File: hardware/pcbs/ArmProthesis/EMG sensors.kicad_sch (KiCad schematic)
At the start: 25 parts, among them IC1 INA128, U1 OPA2188AIDR, U4 OPA188AIDR

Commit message: BMS v0.3 + main folder reconstruction
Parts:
- removed C1: 8.2nF, Capacitor_SMD:C_0603_1608Metric_Pad1.08x0.95mm_HandSolder, symbol Device:C
- removed C2: 1uF, Capacitor_SMD:C_0603_1608Metric_Pad1.08x0.95mm_HandSolder, symbol Device:C
- removed D1, D3: BAT54W, Package_TO_SOT_SMD:SOT-323_SC-70, symbol Diode:BAT54W
- removed U1: OPA2188AIDR, OP AMPS:ОПА2188AIDR, symbol OP AMPS:OPA2188AIDR
- removed U3: ~, Connector_JST:JST_GH_BM02B-GHS-TBT_1x02-1MP_P1.25mm_Vertical, symbol headers:H_2
- removed U4: OPA188AIDR, OP AMPS:OPA188, symbol OP AMPS:OPA188AIDR
- removed U5: ~, Connector_JST:JST_GH_BM03B-GHS-TBT_1x03-1MP_P1.25mm_Vertical, symbol headers:H_3
- removed U6, U7, U8: ~, EMG:EMG_Snap_4mm, symbol headers:H_1
- added C10, C11, C6, C7, C8, C9: 1uF, Capacitor_SMD:C_0603_1608Metric_Pad1.08x0.95mm_HandSolder, symbol Device:C
- added D1, D3: BAT54J, Diode_SMD:D_SOD-323F, symbol Diode:BAT54J
- added J2, J4: Conn_01x01_Pin, Connectors:DIN_Male_1PIN_1.5mm, symbol Connector:Conn_01x01_Pin
- added J3: Conn_01x03_Pin, Connector_JST:JST_GH_SM03B-GHS-TB_1x03-1MP_P1.25mm_Horizontal, symbol Connector:Conn_01x03_Pin
- added R11: 1M, Resistor_SMD:R_0603_1608Metric_Pad0.98x0.95mm_HandSolder, symbol Device:R
- added U1, U2: ~, EMG:EMG_Snap_4mm, symbol headers:H_1
- added U6: OPA2188AIDR, OP AMPS:ОПА2188AIDR, symbol OP AMPS:OPA2188AIDR
- added U7: OPA188AIDR, OP AMPS:OPA188, symbol OP AMPS:OPA188AIDR
- C3: value 1uF -> 8.2nF; Website https://www.digikey.in/en/products/detail/kyocera-avx/KGM15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 -> https://eu.mouser.com/ProductDetail/KEMET/C0603X822F5JACTU?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
- IC1: footprint OP AMPS:INA128 -> OP AMPS:INA128U
- R1: value 200 -> 10M
- R2: value 10k -> 10M; Website (none) -> https://eu.mouser.com/ProductDetail/TE-Connectivity-Holswor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
- R3: value 10M -> 200
- R5: value 10M -> 10k; Website https://eu.mouser.com/ProductDetail/TE-Connectivity-Holswor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 -> (none)
- R8: value 10k -> 20k
- R9: value 20k -> 10k
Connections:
- net +5.5V: now also C6.1, C7.1, C8.1, J3.1 (Pin_1), U6.8 (V+), U7.7 (V+); no longer C3.1
- net -5.5V: now also C10.1, C11.1, C9.1, J3.2 (Pin_2), U6.4 (V-), U7.4 (V-); no longer C4.1
- net AEMG: now also R10.2, J4.1 (Pin_1), U7.6 (OUT); no longer R10.1
- net GND: now also R1.1, R2.2, C10.2, C11.2, C6.2, C7.2, C8.2, C9.2, J3.3 (Pin_3), R11.1, U6.3 (+INA), U6.5 (+INB), U7.3 (+IN); no longer C4.2, R3.1, R5.2
- net INVERTED: now also R6.1, R8.2, U6.1 (OUTA); no longer R6.2, R9.2
- net Vin1: now also R1.2, U1.1; no longer R3.2
- net Vin2: now also R2.1, U2.1; no longer R5.1
- net at R7.1: now also R9.1, D3.1 (K); no longer R8.2
- net at R7.2: now also R6.2, D1.2 (A), U6.6 (-INB); no longer R6.1
- net at IC1.1: now also R3.2; no longer R1.2
- net at IC1.6: now also R4.1; no longer R2.1
- net at IC1.8: now also R3.1; no longer R1.1
- net at R4.2: now also C3.1, C4.2
- net at VR1.1, VR1.2: now also R5.1, U6.2 (-INA); no longer R4.1
- new net: J2.1 (Pin_1), R11.2
- new net: D1.1 (K), D3.2 (A), U6.7 (OUTB)
- new net: R10.1, R8.1, R9.2, U7.2 (-IN)
- new net: C4.1, R5.2

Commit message: .
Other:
- note added: "Amplifiers"
- note added: "Decoupling capacitors for each amplifier"
- note added: "Headers and connectors"
- moved on the sheet: C10, C11, C6, C7, C8, C9, J2, J3, J4, R11, U1, U2

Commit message: .
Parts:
- removed C3: 8.2nF, Capacitor_SMD:C_0603_1608Metric_Pad1.08x0.95mm_HandSolder, symbol Device:C
- removed C4: 1uF, Capacitor_SMD:C_0603_1608Metric_Pad1.08x0.95mm_HandSolder, symbol Device:C
- removed U7: OPA188AIDR, OP AMPS:OPA188, symbol OP AMPS:OPA188AIDR
- added C1: 250nF, Resistor_SMD:R_0402_1005Metric, symbol Device:C
- added C2: 100nF, Resistor_SMD:R_0402_1005Metric, symbol Device:C
- added R12: 10k, Resistor_SMD:R_0402_1005Metric, symbol Device:R
- added U3: OPA2188AIDR, OP AMPS:OPA2188, symbol OP AMPS:OPA2188AIDR
- R10, R3, R6, R7, R8, R9: footprint Resistor_SMD:R_0603_1608Metric_Pad0.98x0.95mm_HandSolder -> Resistor_SMD:R_0402_1005Metric
- R4: value 10k -> 33k; footprint Resistor_SMD:R_0603_1608Metric_Pad0.98x0.95mm_HandSolder -> Resistor_SMD:R_0402_1005Metric
- R5: value 10k -> 3.16k; footprint Resistor_SMD:R_0603_1608Metric_Pad0.98x0.95mm_HandSolder -> Resistor_SMD:R_0402_1005Metric
- U6: footprint OP AMPS:ОПА2188AIDR -> OP AMPS:OPA2188
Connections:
- net +5.5V: now also U3.8 (V+)
- net -5.5V: now also U3.4 (V-)
- net AEMG: now also C2.1, U3.1 (OUTA), U3.2 (-INA); no longer R10.2
- net GND: now also C1.1, U3.5 (+INB)
- net at IC1.6: now also R12.1; no longer R4.1
- net at R4.2: now also R5.1, C1.2, C2.2
- net at R10.1, R8.1, R9.2: now also U3.6 (-INB)
- net at U6.2 (-INA), VR1.1, VR1.2: now also R12.2; no longer R5.1
- net at R5.2: now also U3.3 (+INA)
- new net non-filtered: R10.2, R4.1, U3.7 (OUTB)
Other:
- moved on the sheet: D1, D3, IC1, R1, R10, R2, R3, R6, R7, R8, R9, U6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

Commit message: updates
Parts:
- removed C2: 100nF, Resistor_SMD:R_0402_1005Metric, symbol Device:C
- removed D1, D3: BAT54J, Diode_SMD:D_SOD-323F, symbol Diode:BAT54J
- removed R6, R7: 20k, Resistor_SMD:R_0402_1005Metric, symbol Device:R
- added C3: 100nF, Resistor_SMD:R_0402_1005Metric, symbol Device:C
- C1: value 250nF -> 100nF; LCSC (none) -> C307331
- C10, C11, C6, C7, C8, C9: footprint Capacitor_SMD:C_0603_1608Metric_Pad1.08x0.95mm_HandSolder -> Resistor_SMD:R_0603_1608Metric; LCSC (none) -> C15849
- IC1: LCSC (none) -> C22233
- J3: LCSC (none) -> C514175
- R1, R2: footprint Resistor_SMD:R_0603_1608Metric_Pad0.98x0.95mm_HandSolder -> Resistor_SMD:R_0603_1608Metric; LCSC (none) -> C7250
- R10: value 20k -> 10kΩ; LCSC (none) -> C25850
- R11: footprint Resistor_SMD:R_0603_1608Metric_Pad0.98x0.95mm_HandSolder -> Resistor_SMD:R_0603_1608Metric; LCSC (none) -> C22935
- R12: LCSC (none) -> C25744
- R3: LCSC (none) -> C25087
- R4: value 33k -> 6.8kΩ; LCSC (none) -> C25917
- R5: value 3.16k -> 75kΩ; LCSC (none) -> C25798
- R8: value 20k -> 6.8k; LCSC (none) -> C25917
- R9: value 10k -> 10.5kΩ; LCSC (none) -> C173943
- U3, U6: LCSC (none) -> C17271
- VR1: LCSC (none) -> C48084
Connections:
- net +5.5V: no longer IC1.7 (V+), U3.8 (V+), U6.8 (V+)
- net -5.5V: no longer IC1.4 (V-), U3.4 (V-), U6.4 (V-)
- net AEMG: now also R8.1, R9.2; no longer U3.2 (-INA)
- net GND: now also R10.1, R5.1; no longer U3.5 (+INB)
- net INVERTED: now also U3.5 (+INB); no longer R8.2
- net non-filtered: now also U3.6 (-INB); no longer R10.2
- net at R5.2, U3.3 (+INA): now also C1.2, C3.1
- net FB: now reaches R9.1
- net FB: now also R10.2, U3.2 (-INA)
- new net: C3.2, R4.2, R8.2
- new net +5V: IC1.7 (V+), U3.8 (V+), U6.8 (V+)
- new net -5V: IC1.4 (V-), U3.4 (V-), U6.4 (V-)
- no-connect marks 0 -> 2
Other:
- moved on the sheet: C1, C10, C11, C6, C7, C8, C9, R4, R5, U3

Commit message: Fixed EMG sensors active band pass filter
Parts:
- C1: value 100nF -> 7.87uF
- C3: value 100nF -> 316nF
- R10: value 10kΩ -> 1k
- R4: value 6.8kΩ -> 1k
- R5: value 75kΩ -> 1k
- R8: value 6.8k -> 1k
- R9: value 10.5kΩ -> 10k
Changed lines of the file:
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@@
 			)
 		)
-		(property "Value" "75kΩ"
+		(property "Value" "1k"
 			(at 209.296 109.474 0)
 			(effects
@@
 			)
 		)
-		(property "Value" "6.8k"
+		(property "Value" "1k"
 			(at 229.87 94.234 90)
 			(effects
@@
 			)
 		)
-		(property "Value" "10.5kΩ"
+		(property "Value" "10k"
 			(at 267.716 115.316 0)
 			(effects
@@
 			)
 		)
-		(property "Value" "6.8kΩ"
+		(property "Value" "1k"
 			(at 191.262 108.966 90)
 			(effects
@@
 			)
 		)
-		(property "Value" "100nF"
+		(property "Value" "7.87uF"
 			(at 202.184 117.602 0)
 			(effects
@@
 			)
 		)
-		(property "Value" "100nF"
+		(property "Value" "316nF"
 			(at 203.454 107.188 90)
 			(effects
@@
 			)
 		)
-		(property "Value" "10kΩ"
+		(property "Value" "1k"
 			(at 267.97 123.444 0)
 			(effects

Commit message: Fixed LCSC numbers of the new filter parts
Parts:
- C1: LCSC C307331 -> C6119763
- C3: LCSC C307331 -> C47118439
- R10: LCSC C25850 -> C106235
- R4, R8: LCSC C25917 -> C106235
- R5: LCSC C25798 -> C106235
- R9: LCSC C173943 -> C25744
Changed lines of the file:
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@@
 			)
 		)
-		(property "LCSC" "C25798"
+		(property "LCSC" "C106235"
 			(at 209.296 115.57 0)
 			(effects
@@
 			)
 		)
-		(property "LCSC" "C25917"
+		(property "LCSC" "C106235"
 			(at 229.87 98.298 90)
 			(effects
@@
 			)
 		)
-		(property "LCSC" "C173943"
+		(property "LCSC" "C25744"
 			(at 262.89 114.046 0)
 			(effects
@@
 			)
 		)
-		(property "LCSC" "C25917"
+		(property "LCSC" "C106235"
 			(at 191.262 111.506 90)
 			(effects
@@
 			)
 		)
-		(property "LCSC" "C307331"
+		(property "LCSC" "C6119763"
 			(at 204.216 115.57 0)
 			(effects
@@
 			)
 		)
-		(property "LCSC" "C307331"
+		(property "LCSC" "C47118439"
 			(at 200.406 111.506 90)
 			(effects
@@
 			)
 		)
-		(property "LCSC" "C25850"
+		(property "LCSC" "C106235"
 			(at 262.89 121.666 0)
 			(effects

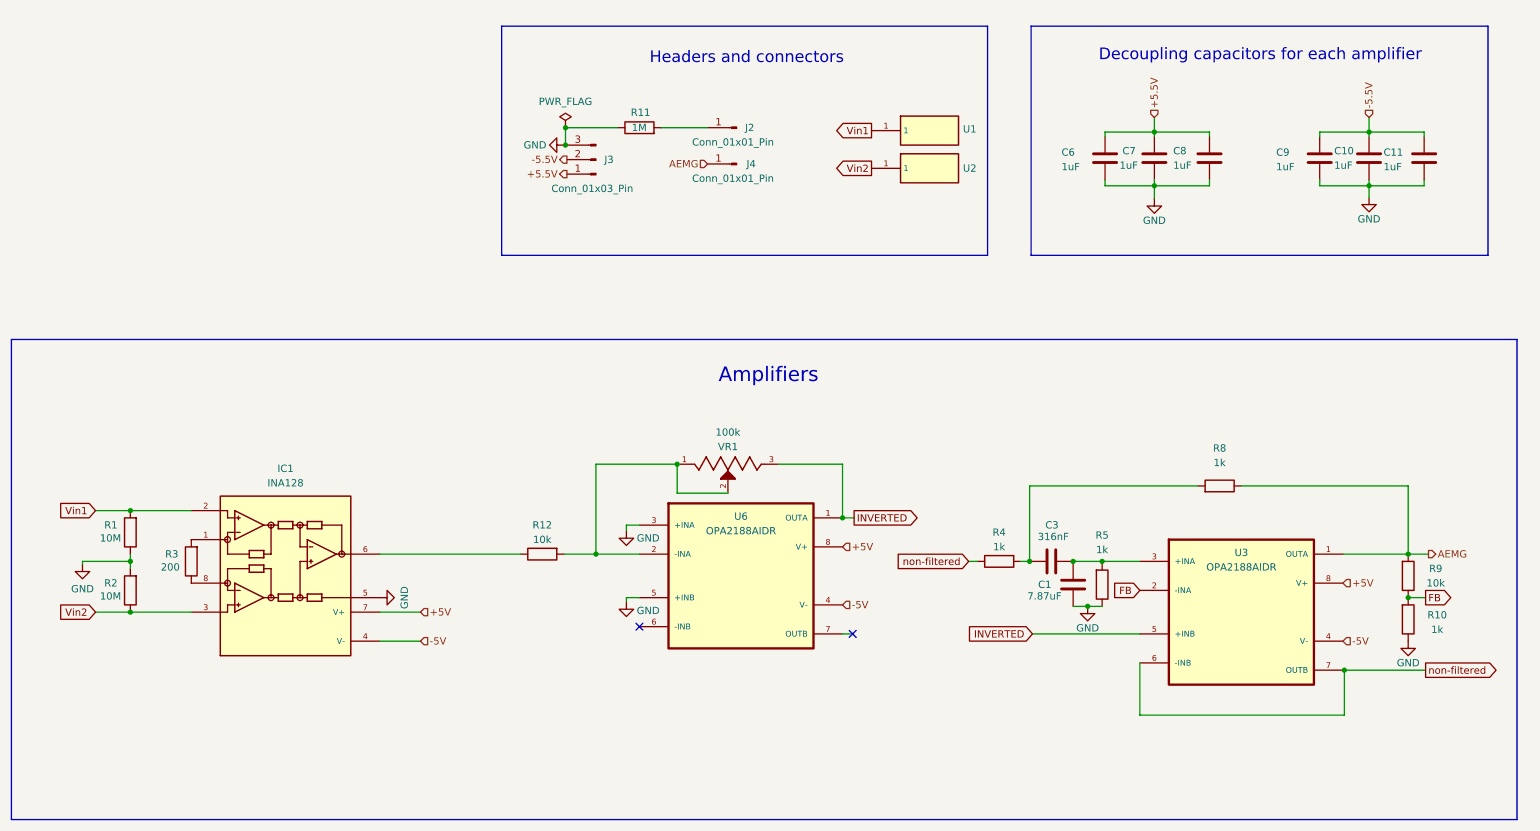
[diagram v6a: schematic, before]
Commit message: Fixed compatibility of connectors  + new BMS chip
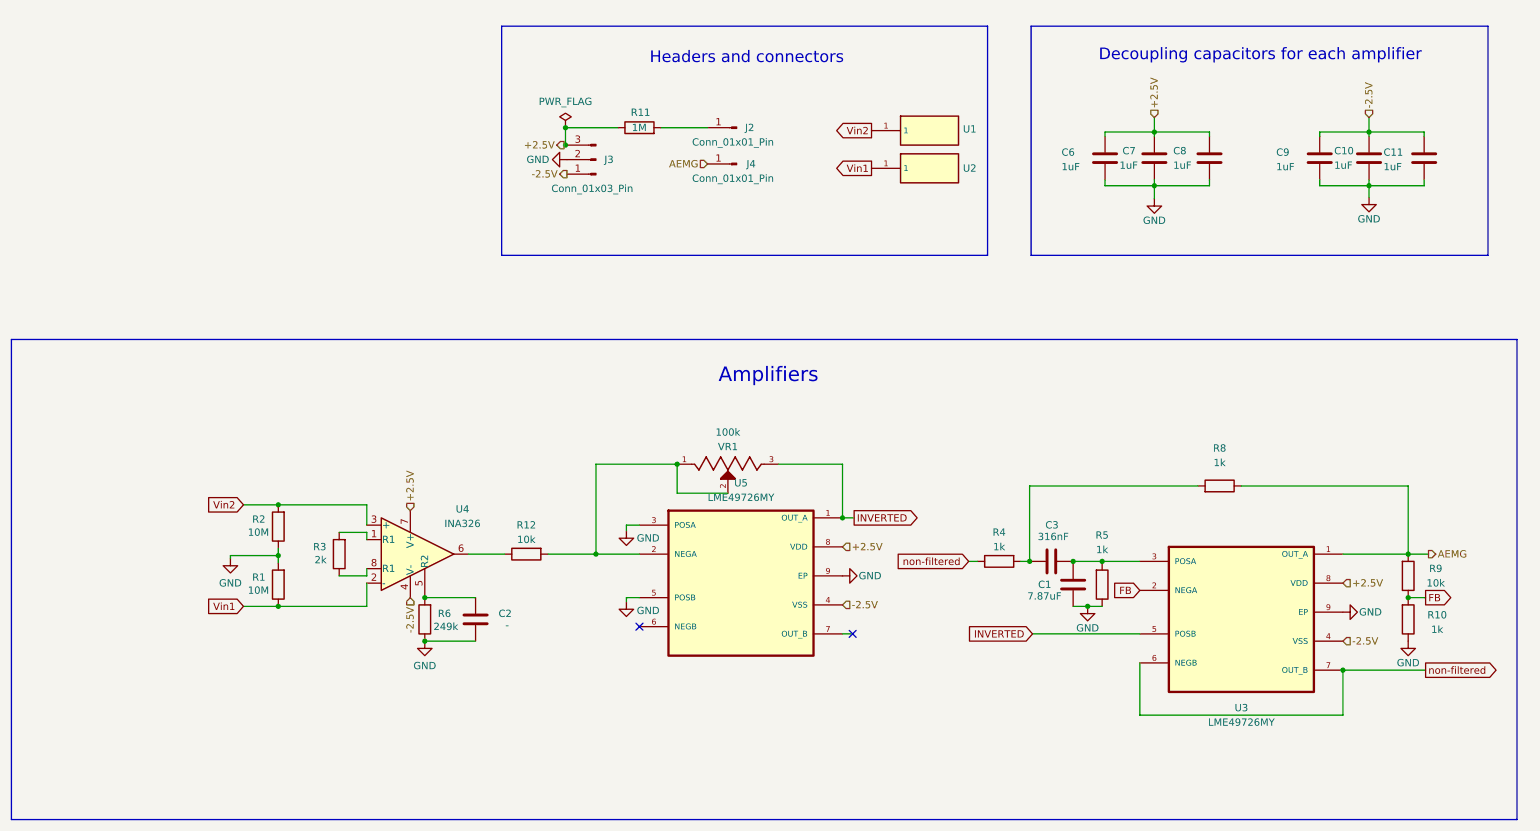
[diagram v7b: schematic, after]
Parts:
- removed IC1: INA128, OP AMPS:INA128U, symbol OP AMPS:INA128
- removed U3, U6: OPA2188AIDR, OP AMPS:OPA2188, symbol OP AMPS:OPA2188AIDR
- added C2: -, Capacitor_SMD:C_0603_1608Metric, symbol Device:C
- added R6: 249k, Resistor_SMD:R_0402_1005Metric, symbol Device:R
- added U3, U5: LME49726MY, OP AMPS:LME49726MY, symbol OP AMPS:LME49726MY
- added U4: INA326, Package_SO:MSOP-8_3x3mm_P0.65mm, symbol Amplifier_Instrumentation:INA326
- R3: value 200 -> 2k; LCSC C25087 -> C60488
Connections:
- net AEMG: now also U3.1 (OUT_A)
- net FB: now also U3.2 (NEGA)
- net GND: now also J3.2 (Pin_2), R1.2, R2.1, C2.1, R6.1, U3.9 (EP), U5.3 (POSA), U5.5 (POSB), U5.9 (EP); no longer J3.3 (Pin_3), R1.1, R11.1, R2.2
- net INVERTED: now also U3.5 (POSB), U5.1 (OUT_A)
- net Vin1: now also R1.1, U2.1, U4.2 (-); no longer R1.2, U1.1
- net Vin2: now also R2.2, U1.1, U4.3 (+); no longer R2.1, U2.1
- net non-filtered: now also U3.6 (NEGB), U3.7 (OUT_B)
- net at R12.1: now also U4.6
- net at R12.2, VR1.1, VR1.2: now also U5.2 (NEGA)
- net at R3.1: now also U4.8 (R1)
- net at R3.2: now also U4.1 (R1)
- net at C1.2, C3.1, R5.2: now also U3.3 (POSA)
- net +5.5V renamed +2.5V
- net +2.5V: now also J3.3 (Pin_3), R11.1, U3.8 (VDD), U4.7 (V+), U5.8 (VDD); no longer J3.1 (Pin_1)
- net -5.5V renamed -2.5V
- net -2.5V: now also J3.1 (Pin_1), U3.4 (VSS), U4.4 (V-), U5.4 (VSS); no longer J3.2 (Pin_2)
- new net: C2.2, R6.2, U4.5 (R2)
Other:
- moved on the sheet: R1, R12, R2, R3

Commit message: Ordered versions
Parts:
- removed J4: Conn_01x01_Pin, Connectors:DIN_Male_1PIN_1.5mm, symbol Connector:Conn_01x01_Pin
- added J1: Conn_01x02_Pin, Connector_JST:JST_GH_SM02B-GHS-TB_1x02-1MP_P1.25mm_Horizontal, symbol Connector:Conn_01x02_Pin
- C1: value 7.87uF -> 10uF; footprint Resistor_SMD:R_0402_1005Metric -> Capacitor_SMD:C_0402_1005Metric
- C10, C11, C6, C7, C8, C9: footprint Resistor_SMD:R_0603_1608Metric -> Capacitor_SMD:C_0603_1608Metric
- C2: value - -> DNP; LCSC C6119763 -> (none)
- C3: value 316nF -> 330nF; footprint Resistor_SMD:R_0402_1005Metric -> Capacitor_SMD:C_0402_1005Metric
- J2: value Conn_01x01_Pin -> DNP
- R6: LCSC C2984416 -> C226368
- U1, U2: value ~ -> DNP
- U3, U5: LCSC (none) -> C128880
- U4: LCSC (none) -> C179740
- VR1: footprint Trimmers:TRIM_3296W-1-104ALF -> Potentiometer_THT:Potentiometer_Bourns_3296W_Vertical
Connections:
- net AEMG: now also J1.1 (Pin_1), J1.2 (Pin_2)
